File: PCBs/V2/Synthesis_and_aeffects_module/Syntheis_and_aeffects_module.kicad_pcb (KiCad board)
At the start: 2 copper layers, 83.5 x 60 mm, 19 parts, among them J1 AudioJack3_SwitchTR, U1 STM32H750VBTx

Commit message: pcb progress
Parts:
- added C6(decoupleamp)1: 0.1uf, Capacitor_SMD:C_0603_1608Metric_Pad1.08x0.95mm_HandSolder, F.Cu at (128.5, 114.0)
- added Debug1: Conn_01x01, TestPoint:TestPoint_Pad_1.5x1.5mm, F.Cu at (151.5, 93.0)
- added Debug2: Conn_01x01, TestPoint:TestPoint_Pad_1.5x1.5mm, F.Cu at (93.5, 71.0)
- added Debug3: Conn_01x01, TestPoint:TestPoint_Pad_1.5x1.5mm, F.Cu at (82.5, 74.5)
- added Debug4: Conn_01x01, TestPoint:TestPoint_Pad_1.5x1.5mm, F.Cu at (86.5, 82.0)
- added J2: IN, Connector_PinHeader_2.54mm:PinHeader_1x05_P2.54mm_Vertical, F.Cu at (115.9, 99.3)
- added J3: OUT, Connector_PinHeader_2.54mm:PinHeader_1x05_P2.54mm_Vertical, F.Cu at (120.5, 99.3)
- added U2: TPA6110A2DGN, Package_SO:HVSSOP-8-1EP_3x3mm_P0.65mm_EP1.57x1.89mm, F.Cu at (90.3, 89.0)
- C1, C2, C3, C4, C5, C8, C9: value C -> 0.1uf; footprint Capacitor_THT:CP_Radial_D5.0mm_P2.00mm -> Capacitor_SMD:C_0603_1608Metric_Pad1.08x0.95mm_HandSolder
- C6(VCAP)1: renamed from C6; footprint Capacitor_THT:CP_Radial_D5.0mm_P2.00mm -> Capacitor_SMD:C_0603_1608Metric_Pad1.08x0.95mm_HandSolder
- C7(VCAP)2: renamed from C7; footprint Capacitor_THT:CP_Radial_D5.0mm_P2.00mm -> Capacitor_SMD:C_0603_1608Metric_Pad1.08x0.95mm_HandSolder
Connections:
- J1 pad R: /DAC_OUT2 -> unconnected-(J1-PadR)
- J1 pad T: /DAC_OUT1 -> Net-(C(c)output1-Pad2)
- U1 pad 25: /DAC_OUT2 -> unconnected-(U1-PA3-Pad25)
- U1 pad 29: unconnected-(U1-PA5-Pad29) -> /DAC_OUT2
- U1 pad 46: unconnected-(U1-PB10-Pad46) -> /USART1_COMM_INPUT_RX
- U1 pad 51: /UART5_COMM_RX -> unconnected-(U1-PB12-Pad51)
- U1 pad 52: /UART5_COMM_TX -> unconnected-(U1-PB13-Pad52)
- U1 pad 68: unconnected-(U1-PA9-Pad68) -> /USART1_MIDI_TX
- U1 pad 69: unconnected-(U1-PA10-Pad69) -> /USART1_MIDI_RX
- U1 pad 70: /UART_MIDI_RX -> unconnected-(U1-PA11-Pad70)
- U1 pad 71: /UART_MIDI_TX -> unconnected-(U1-PA12-Pad71)
- U1 pad 77: unconnected-(U1-PA15-Pad77) -> /MISC_3
- U1 pad 78: unconnected-(U1-PC10-Pad78) -> /USART3_MIDI_TX
- U1 pad 79: /MISC_3 -> /USART3_MIDI_RX
- U1 pad 86: unconnected-(U1-PD5-Pad86) -> /USART2_COMM_OUTPUT_TX
- U1 pad 87: unconnected-(U1-PD6-Pad87) -> /USART2_COMM_OUTPUT_RX
- U1 pad 96: unconnected-(U1-PB9-Pad96) -> /USART1_COMM_INPUT_TX

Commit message: schematic progress
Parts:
- added C(c)output1: 220uf, Capacitor_THT:CP_Radial_D5.0mm_P2.00mm, F.Cu at (83.8, 89.4)
- added C(c)output2: 220uf, Capacitor_THT:CP_Radial_D5.0mm_P2.00mm, F.Cu at (83.8, 96.0)
- added Cbypass1: 0.47uf(LOW ESR), Capacitor_SMD:C_0603_1608Metric_Pad1.08x0.95mm_HandSolder, F.Cu at (83.6, 100.5)
- added Cinput1: 0.47uf, Capacitor_SMD:C_0603_1608Metric_Pad1.08x0.95mm_HandSolder, F.Cu at (83.6, 103.0)
- added Cinput2: 0.47uf, Capacitor_SMD:C_0603_1608Metric_Pad1.08x0.95mm_HandSolder, F.Cu at (83.6, 105.5)
- added Rf(40k)1: 40k, Resistor_THT:R_Axial_DIN0207_L6.3mm_D2.5mm_P10.16mm_Horizontal, F.Cu at (69.3, 85.0)
- added Rf(40k)2: 40k, Resistor_THT:R_Axial_DIN0207_L6.3mm_D2.5mm_P10.16mm_Horizontal, F.Cu at (69.7, 92.2)
- added Ri(20k)1: 20k, Resistor_THT:R_Axial_DIN0207_L6.3mm_D2.5mm_P10.16mm_Horizontal, F.Cu at (69.7, 96.2)
- added Ri(20k)2: 20k, Resistor_THT:R_Axial_DIN0207_L6.3mm_D2.5mm_P10.16mm_Horizontal, F.Cu at (69.7, 100.3)
- moved Debug1 43.5 mm to (108.1, 91.3)
- moved C6(decoupleamp)1 39.9 mm to (94.9, 92.3)
- moved MISC3 39.9 mm to (111.6, 98.4)
- moved MISC1 39.9 mm to (111.6, 91.3)
- moved MISC2 37.2 mm to (111.6, 94.8)
- moved J1 36.1 mm to (79.5, 72.3)
- moved Debug3 35.0 mm to (108.1, 98.4)
- moved C7(VCAP)2 31.1 mm to (94.9, 94.9)
- moved Debug4 29.4 mm to (108.1, 102.0)
- moved Debug2 27.9 mm to (108.1, 94.8)
- moved C8 23.2 mm to (94.9, 84.8)
- moved C9 22.7 mm to (94.9, 87.3)
- moved U1 21.3 mm to (110.0, 77.5)
- moved U2 20.5 mm to (100.8, 106.7)
- moved J3 18.1 mm to (104.0, 91.8)
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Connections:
- C6(decoupleamp)1 pad 1: unconnected-(C6(decoupleamp)1-Pad1) -> /VCC
- C6(decoupleamp)1 pad 2: unconnected-(C6(decoupleamp)1-Pad2) -> Net-(U2-VDD)
- J1 pad R: unconnected-(J1-PadR) -> Net-(C(c)output2-Pad2)
- U2 pad 3: GNDPWR -> /VCC
- U2 pad 4: Net-(U2-IN2-) -> Net-(U2-IN1-)
- U2 pad 6: /VCC -> Net-(U2-VDD)
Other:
- board size 83.5 x 60 mm -> 87.5 x 52 mm

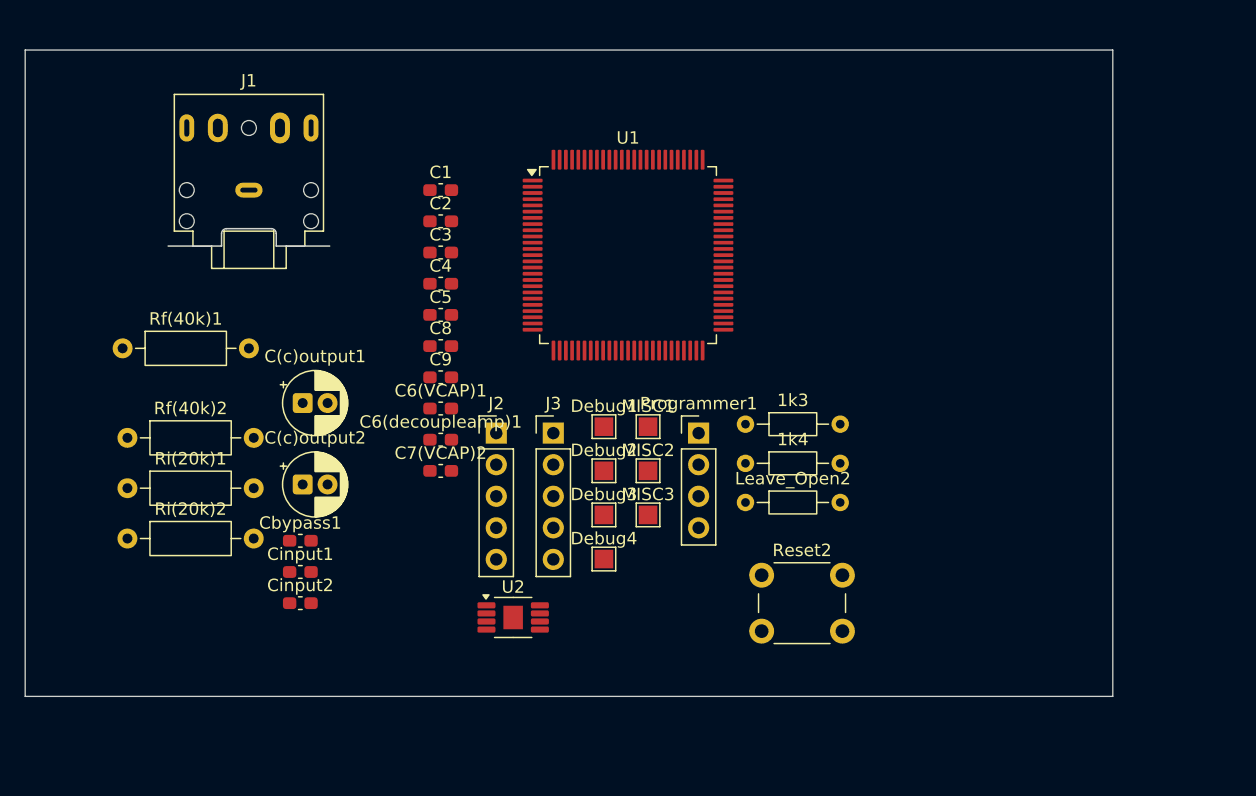
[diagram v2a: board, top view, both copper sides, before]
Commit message: remove adiojack from schematic, replace with pin headers
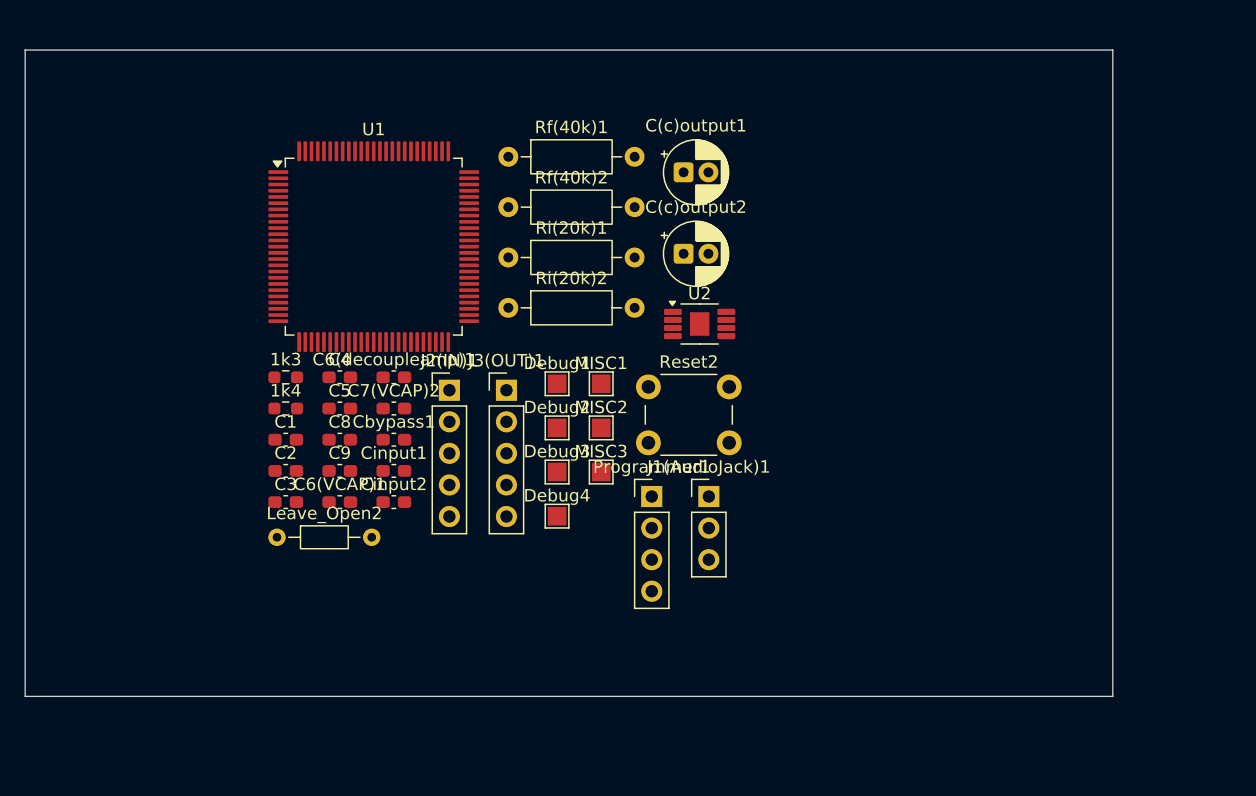
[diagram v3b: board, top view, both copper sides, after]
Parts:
- removed J1: AudioJack3_SwitchTR, Connector_Audio:Jack_3.5mm_CUI_SJ1-3525N_Horizontal
- removed J2: IN, Connector_PinHeader_2.54mm:PinHeader_1x05_P2.54mm_Vertical
- removed J3: OUT, Connector_PinHeader_2.54mm:PinHeader_1x05_P2.54mm_Vertical
- added J1(AudioJack)1: Conn_01x03, Connector_PinHeader_2.54mm:PinHeader_1x03_P2.54mm_Vertical, F.Cu at (116.5, 96.9)
- added J2(IN)1: IN, Connector_PinHeader_2.54mm:PinHeader_1x05_P2.54mm_Vertical, F.Cu at (95.6, 88.4)
- added J3(OUT)1: OUT, Connector_PinHeader_2.54mm:PinHeader_1x05_P2.54mm_Vertical, F.Cu at (100.2, 88.4)
- 1k3, 1k4: footprint Resistor_THT:R_Axial_DIN0204_L3.6mm_D1.6mm_P7.62mm_Horizontal -> Resistor_SMD:R_0603_1608Metric_Pad0.98x0.95mm_HandSolder
- moved Leave_Open2 37.8 mm to (81.8, 100.2)
- moved 1k4 37.3 mm to (82.5, 89.8)
- moved 1k3 37.2 mm to (82.5, 87.3)
- moved C(c)output1 35.8 mm to (114.5, 70.8)
- moved C(c)output2 35.8 mm to (114.5, 77.4)
- moved Rf(40k)2 35.8 mm to (100.4, 73.6)
- moved Ri(20k)1 35.8 mm to (100.4, 77.7)
- moved Ri(20k)2 35.8 mm to (100.4, 81.7)
- moved Rf(40k)1 34.6 mm to (100.4, 69.6)
- moved U2 28.0 mm to (115.8, 83.0)
- moved C1 23.6 mm to (82.5, 92.3)
- moved C2 23.6 mm to (82.5, 94.9)
- moved C3 23.6 mm to (82.5, 97.4)
- moved U1 20.5 mm to (89.5, 76.8)
- moved Reset2 17.7 mm to (111.6, 88.1)
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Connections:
- C(c)output1 pad 2: Net-(C(c)output1-Pad2) -> /AudioJack_T
- C(c)output2 pad 2: Net-(C(c)output2-Pad2) -> /AudioJack_R

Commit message: more progress on synthesis pcb
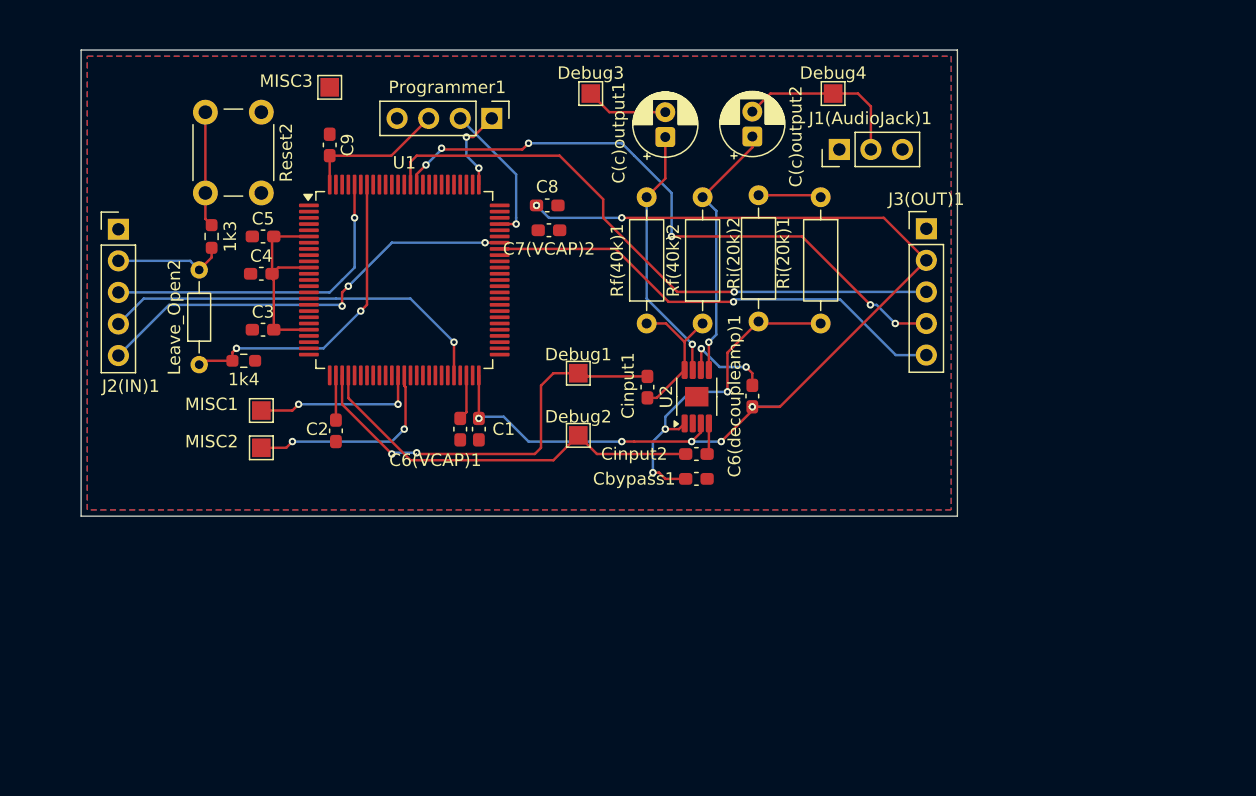
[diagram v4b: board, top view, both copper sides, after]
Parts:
- moved Debug4 40.6 mm to (126.5, 64.5)
- moved Reset2 38.2 mm to (80.5, 66.0), turned to -90 degrees
- moved MISC3 37.9 mm to (86.0, 64.0), turned to 180 degrees
- moved J3(OUT)1 36.2 mm to (134.0, 75.4)
- moved Programmer1 33.0 mm to (99.0, 66.5), turned to -90 degrees
- moved Debug3 30.6 mm to (107.0, 64.5)
- moved J1(AudioJack)1 29.8 mm to (127.0, 69.0), turned to 90 degrees
- moved J2(IN)1 29.6 mm to (69.0, 75.4)
- moved C6(decoupleamp)1 28.9 mm to (120.0, 88.8), turned to 90 degrees
- moved MISC1 27.4 mm to (80.5, 90.0), turned to 180 degrees
- moved MISC2 27.4 mm to (80.5, 93.0), turned to 180 degrees
- moved C9 26.2 mm to (86.0, 68.6), turned to -90 degrees
- moved Ri(20k)1 25.6 mm to (125.5, 72.8), turned to -90 degrees
- moved C8 25.2 mm to (103.5, 73.5), turned to 180 degrees
- moved Cinput2 24.6 mm to (115.5, 93.5)
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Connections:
- C(c)output1 pad 1: Net-(Debug3-Pin_1) -> Net-(U2-VO1)
- C(c)output2 pad 1: Net-(Debug4-Pin_1) -> Net-(U2-VO2)
- Cinput1 pad 1: /DAC_OUT2 -> /DAC_OUT1
- Cinput2 pad 1: /DAC_OUT1 -> /DAC_OUT2
- Cinput2 pad 2: Net-(U2-IN1-) -> Net-(U2-IN2-)
- Debug3 pad 1: Net-(Debug3-Pin_1) -> /AudioJack_T
- Debug4 pad 1: Net-(Debug4-Pin_1) -> /AudioJack_R
- Rf(40k)1 pad 2: Net-(Debug3-Pin_1) -> Net-(U2-VO1)
- Rf(40k)2 pad 2: Net-(Debug4-Pin_1) -> Net-(U2-VO2)
- U2 pad 4: Net-(U2-IN1-) -> Net-(U2-IN2-)
- U2 pad 5: Net-(Debug4-Pin_1) -> Net-(U2-VO2)
- U2 pad 7: Net-(Debug3-Pin_1) -> Net-(U2-VO1)
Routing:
- net /VCC: track 0.00 -> 124.4 mm, vias 0 -> 7
- net /USART2_COMM_OUTPUT_TX: track 0.00 -> 51.1 mm, vias 0 -> 6
- net /USART2_COMM_OUTPUT_RX: track 0.00 -> 49.0 mm, vias 0 -> 1
- net /USART1_MIDI_TX: track 0.00 -> 38.1 mm, vias 0 -> 1
- net /USART1_MIDI_RX: track 0.00 -> 35.2 mm, vias 0 -> 3
- net /DAC_OUT1: track 0.00 -> 34.4 mm, vias 0 -> 2
- net /DAC_OUT2: track 0.00 -> 32.5 mm
- net /USART1_COMM_INPUT_RX: track 0.00 -> 32.0 mm, vias 0 -> 1
- net Net-(U2-BYPASS): track 0.00 -> 27.1 mm, vias 0 -> 3
- net /USART1_COMM_INPUT_TX: track 0.00 -> 26.5 mm, vias 0 -> 1
- net Net-(U1-BOOT0): track 0.00 -> 25.6 mm, vias 0 -> 2
- net Net-(U2-VO2): track 0.00 -> 20.5 mm, vias 0 -> 1
- net Net-(U2-VO1): track 0.00 -> 20.2 mm, vias 0 -> 1
- net /MISC_2: track 0.00 -> 16.5 mm, vias 0 -> 2
- net Net-(U2-IN1-): track 0.00 -> 16.3 mm
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- added copper zone on B.Cu, net GNDPWR
- added copper zone on F.Cu, net GNDPWR
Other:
- board size 87.5 x 52 mm -> 70.5 x 37.5 mm

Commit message: some updates
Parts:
- removed Debug3, Debug4: Conn_01x01, TestPoint:TestPoint_Pad_1.5x1.5mm
- moved Cbypass1 26.2 mm to (123.5, 70.5)
- moved C(c)output1 24.7 mm to (105.5, 91.5), turned to 0 degrees
- moved J1(AudioJack)1 24.2 mm to (118.0, 91.5)
- moved C(c)output2 22.0 mm to (105.5, 84.5), turned to 0 degrees
- moved C6(decoupleamp)1 21.4 mm to (118.5, 67.5), turned to -90 degrees
- moved Ri(20k)2 18.4 mm to (110.5, 67.4), turned to -90 degrees
- moved Cinput2 16.0 mm to (107.0, 80.0)
- moved Ri(20k)1 15.7 mm to (114.9, 84.5), turned to 0 degrees
- moved Rf(40k)2 15.7 mm to (114.0, 67.4), turned to -90 degrees
- moved U2 15.6 mm to (118.5, 73.6), turned to -90 degrees
- moved Rf(40k)1 13.7 mm to (125.1, 81.0), turned to 180 degrees
- moved Debug2 12.9 mm to (103.0, 79.5)
- moved Debug1 6.02 mm to (102.0, 91.5)
- moved J3(OUT)1 3.00 mm to (131.0, 75.4)
- moved Cinput1 1.13 mm to (112.5, 87.5), turned to 90 degrees
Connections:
- C6(decoupleamp)1 pad 1: /VCC -> GNDPWR
- C6(decoupleamp)1 pad 2: Net-(U2-VDD) -> /VCC
- Cinput1 pad 2: Net-(U2-IN1-) -> Net-(Cinput1-Pad2)
- Cinput2 pad 2: Net-(U2-IN2-) -> Net-(Cinput2-Pad2)
- Rf(40k)2 pad 1: Net-(U2-IN1-) -> Net-(U2-IN2-)
- Ri(20k)1 pad 1: Net-(U2-IN1-) -> Net-(Cinput1-Pad2)
- Ri(20k)1 pad 2: Net-(U2-BYPASS) -> Net-(U2-IN1-)
- Ri(20k)2 pad 1: Net-(U2-BYPASS) -> Net-(U2-IN2-)
- Ri(20k)2 pad 2: Net-(U2-IN1-) -> Net-(Cinput2-Pad2)
- U2 pad 3: /VCC -> GNDPWR
- U2 pad 6: Net-(U2-VDD) -> /VCC
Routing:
- net /VCC: track 124.4 -> 232.2 mm, vias 7 -> 9
- net GNDPWR: track 0.00 -> 25.8 mm, vias 0 -> 76
- net Net-(U2-BYPASS): track 27.1 -> 3.53 mm, vias 3 -> 0
- net /MISC_3: track 0.00 -> 16.2 mm, vias 0 -> 2
- net Net-(U1-NRST): track 9.29 -> 20.4 mm, vias 0 -> 2
- net Net-(U2-VDD): track 7.64 -> 0.00 mm, vias 2 -> 0
- net Net-(U2-IN2-): track 2.52 -> 9.01 mm
- net Net-(U2-IN1-): track 16.3 -> 11.2 mm
- net /USART2_COMM_OUTPUT_TX: track 51.1 -> 46.5 mm, vias 6 -> 3
- net /DAC_OUT2: track 32.5 -> 36.6 mm, vias 0 -> 2
- net /USART2_COMM_OUTPUT_RX: track 49.0 -> 45.1 mm
- net /AudioJack_T: track 6.62 -> 10.5 mm
- net Net-(U2-VO2): track 20.5 -> 16.8 mm, vias 1 -> 0
- net Net-(Cinput2-Pad2): track 0.00 -> 3.64 mm
- net Net-(C7(VCAP)2-Pad1): track 0.00 -> 3.60 mm
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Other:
- board size 70.5 x 37.5 mm -> 68 x 37.5 mm

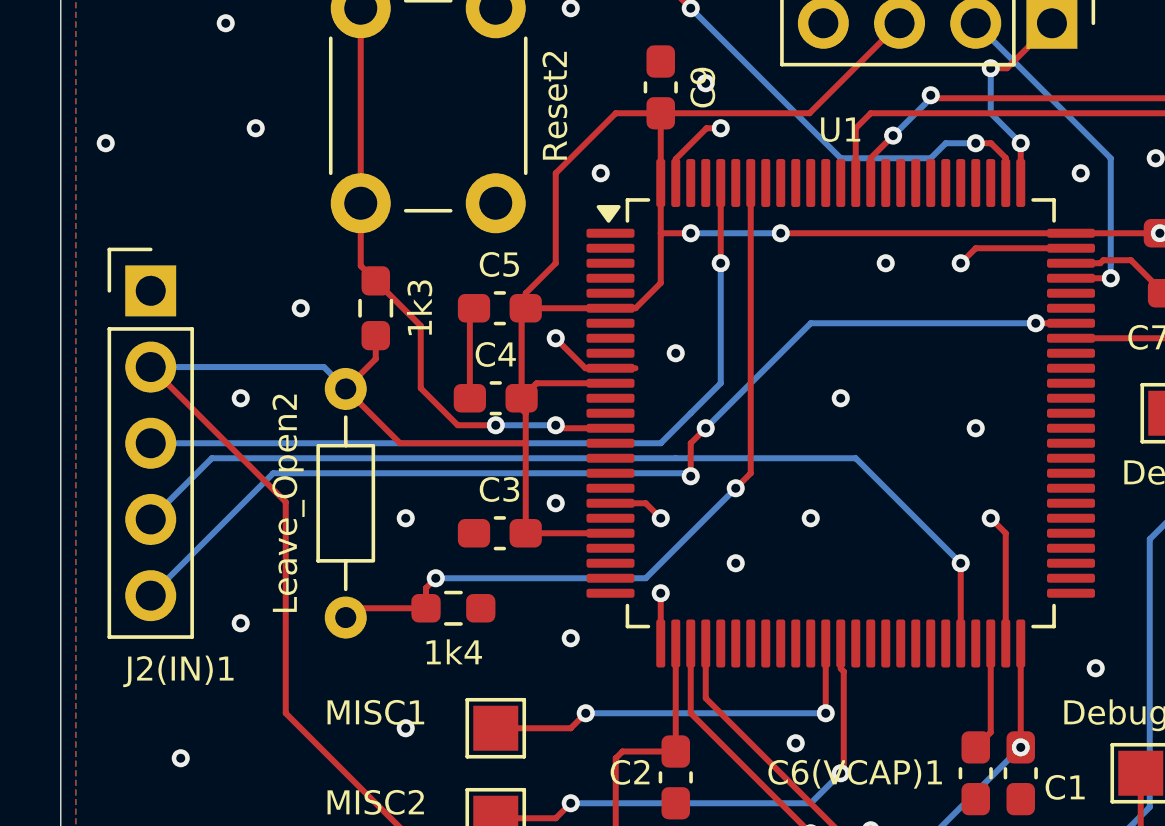
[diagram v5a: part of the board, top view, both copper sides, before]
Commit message: messed UART connection for synthesis PCB :/ good thing i had those misc pads for testing. Need to reorder.
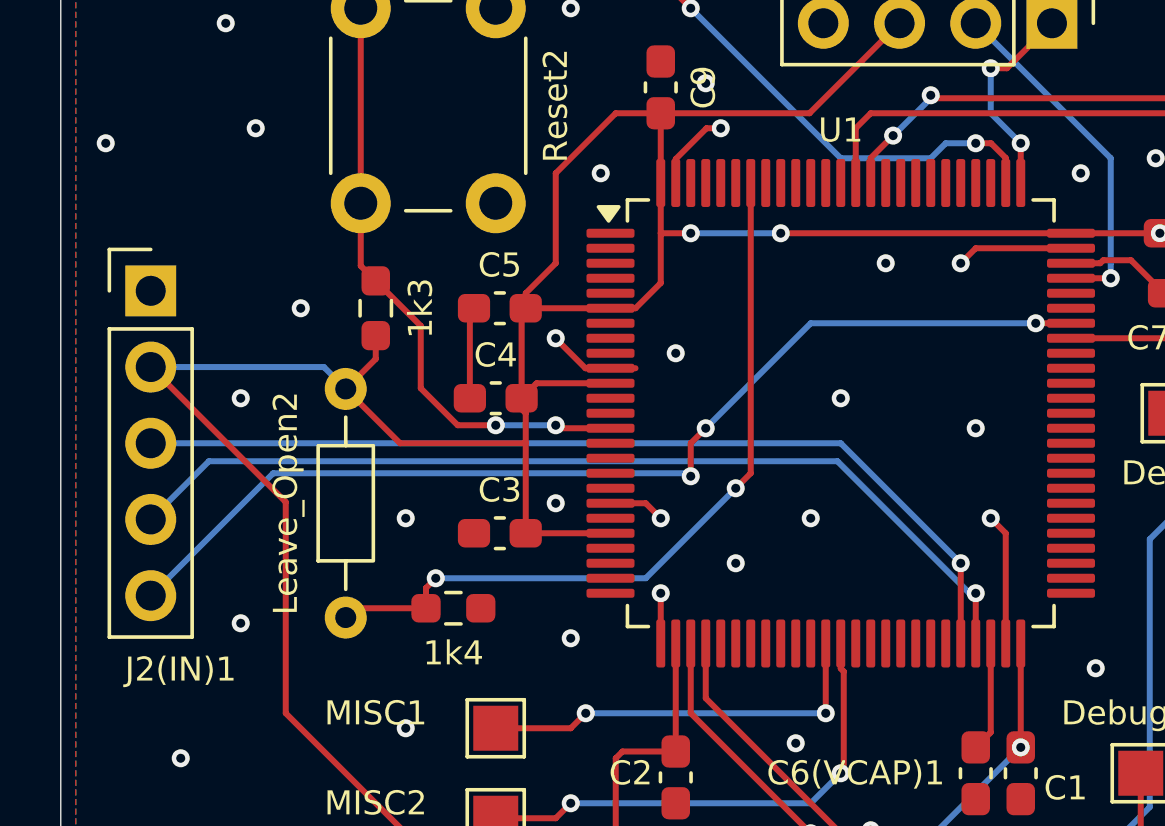
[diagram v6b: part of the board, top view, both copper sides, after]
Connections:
- net GNDPWR renamed /GND
- J2(IN)1 pad 3: /USART1_COMM_INPUT_TX -> /USART3_COMM_INPUT_TX
- J2(IN)1 pad 4: /USART1_COMM_INPUT_RX -> /USART3_COMM_INPUT_RX
- U1 pad 46: /USART1_COMM_INPUT_RX -> /USART3_COMM_INPUT_TX
- U1 pad 47: unconnected-(U1-PB11-Pad47) -> /USART3_COMM_INPUT_RX
- U1 pad 78: /USART3_MIDI_TX -> unconnected-(U1-PC10-Pad78)
- U1 pad 79: /USART3_MIDI_RX -> unconnected-(U1-PC11-Pad79)
- U1 pad 96: /USART1_COMM_INPUT_TX -> unconnected-(U1-PB9-Pad96)
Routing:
- net /USART1_COMM_INPUT_RX: track 32.0 -> 0.00 mm, vias 1 -> 0
- net /USART3_COMM_INPUT_RX: track 0.00 -> 31.8 mm, vias 0 -> 1
- net /USART3_COMM_INPUT_TX: track 0.00 -> 31.3 mm, vias 0 -> 1
- net /USART1_COMM_INPUT_TX: track 26.5 -> 0.00 mm, vias 1 -> 0
